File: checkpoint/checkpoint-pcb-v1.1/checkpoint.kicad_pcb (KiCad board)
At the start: 4 copper layers, 85.2 x 39.6 mm, 111 parts, among them J1 T0, J10 CAN_OUT, J11 BOOT, J12 Y_ENDSTOP, J13 SERVO, J14 RGB, J15 SWD, J16 USB_C_Receptacle_USB2.0_16P, J17 PWR_CAN_IN, J18 PWR_OUT, J19 I2C, J2 T1, J3 T2, J4 T3, J5 2_WIRE, J6 24_3_WIRE_A, J7 PT100, J8 23_WIRE, J9 PT100_1K, Q1 BSS138, SW1 SW_RESET, U1 MAX31865xTP, U2 SN65HVD1050D, U3 STM32G0B1CBTx, U4 USBLC6-2P6, U5 AMS1117-3.3, U6 TPS5430DDA, Y1 Crystal

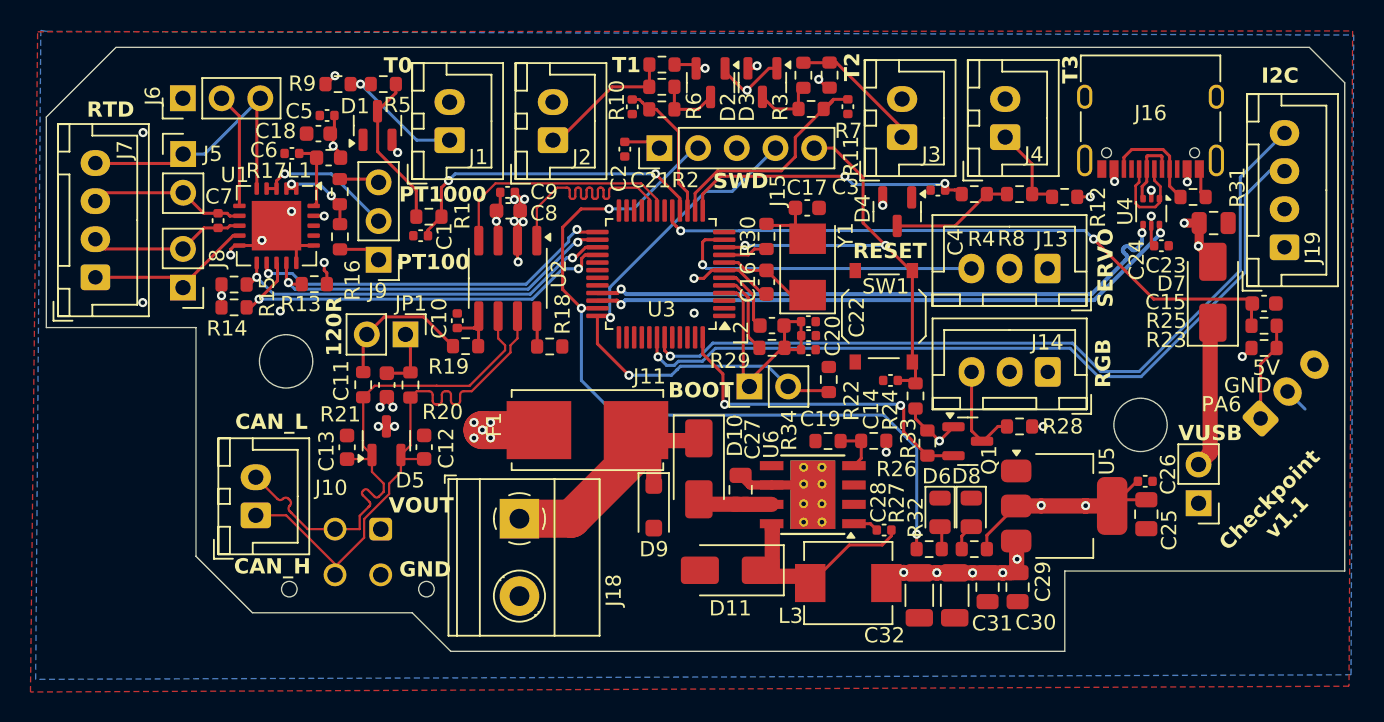
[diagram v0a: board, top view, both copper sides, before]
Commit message: chore: clear space around mount holes
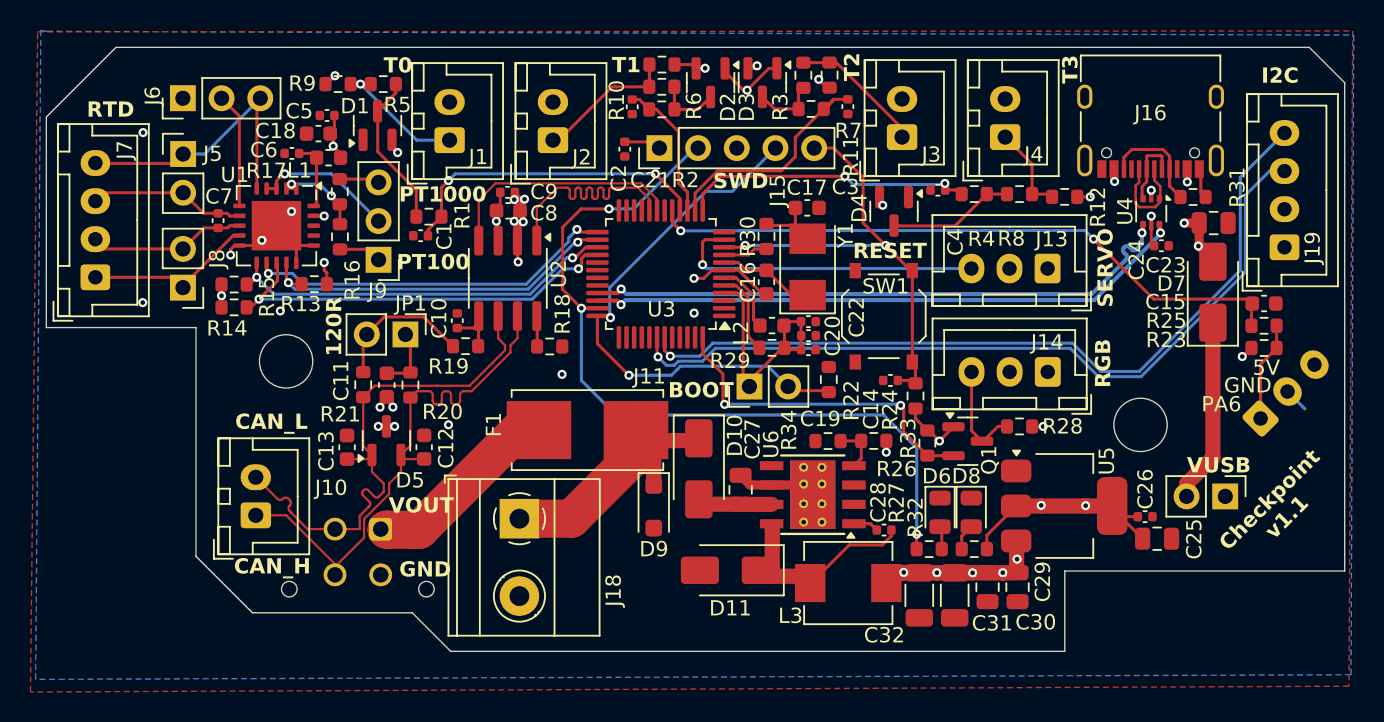
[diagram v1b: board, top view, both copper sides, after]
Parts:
- moved C26 2.32 mm to (94.3, 64.9)
- moved JP2 1.81 mm to (99.5, 63.5), turned to -90 degrees
- moved C25 1.76 mm to (95.1, 66.3), turned to 0 degrees
- moved D4 0.21 mm to (77.8, 44.8)
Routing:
- net VIN: track 3.72 -> 12.7 mm, vias 5 -> 0
- net Net-(D7-K): track 9.62 -> 12.2 mm
- net +3.3V: track 110.3 -> 111.6 mm
- net GND: track 33.8 -> 34.1 mm, vias 19 -> 21
- removed copper zone on In1.Cu, net VIN

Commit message: fix: rotate backwards filter diode
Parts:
- moved D10 0.23 mm to (65.0, 61.9), turned to 90 degrees
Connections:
- C27 pad 1: Net-(D10-A) -> Net-(D10-K)
- D10 pad 1: VOUT -> Net-(D10-K)
- D10 pad 2: Net-(D10-A) -> VOUT
- U6 pad 7: Net-(D10-A) -> Net-(D10-K)
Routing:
- net Net-(D10-K): track 0.00 -> 4.19 mm
- net Net-(D10-A): track 4.19 -> 0.00 mm
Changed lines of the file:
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@@
 	(net 21 "Net-(D4-COM)")
 	(net 22 "Net-(D8-A)")
-	(net 23 "Net-(D10-A)")
+	(net 23 "Net-(D10-K)")
 	(net 24 "Net-(J1-Pin_1)")
 	(net 25 "Net-(J2-Pin_1)")
@@
 		(tags "capacitor")
 		(property "Reference" "C27"
-			(at 3.33 0.79 -90)
+			(at 3.34 0.81 -90)
 			(layer "F.SilkS")
 			(effects
@@
 			(layers "F.Cu" "F.Paste" "F.Mask")
 			(roundrect_rratio 0.25)
-			(net 23 "Net-(D10-A)")
+			(net 23 "Net-(D10-K)")
 			(pintype "passive")
 		)
@@
 	(footprint "Diode_SMD:D_SMA"
 		(layer "F.Cu")
-		(at 64.980408 61.721118 -90)
+		(at 64.980408 61.948618 90)
 		(descr "Diode SMA (DO-214AC)")
 		(tags "Diode SMA (DO-214AC)")
 		(property "Reference" "D10"
-			(at -2.18 -2.37 -90)
+			(at 2.1375 2.35 -90)
 			(layer "F.SilkS")
 			(effects
@@
 		)
 		(property "Value" "SS34"
-			(at 0 2.6 90)
+			(at 0 2.6 -90)
 			(layer "F.Fab")
 			(effects
@@
 		)
 		(property "Footprint" "Diode_SMD:D_SMA"
-			(at 0 0 -90)
+			(at 0 0 90)
 			(unlocked yes)
 			(layer "F.Fab")
@@
 		)
 		(property "Datasheet" ""
-			(at 0 0 -90)
+			(at 0 0 90)
 			(unlocked yes)
 			(layer "F.Fab")
@@
 		)
 		(property "Description" "40V 3A Schottky Diode, SMA"
-			(at 0 0 -90)
+			(at 0 0 90)
 			(unlocked yes)
 			(layer "F.Fab")
@@
 		)
 		(property "Availability" ""
-			(at 0 0 -90)
+			(at 0 0 90)
 			(unlocked yes)
 			(layer "F.Fab")
@@
 		)
 		(property "Check_prices" ""
-			(at 0 0 -90)
+			(at 0 0 90)
 			(unlocked yes)
 			(layer "F.Fab")
@@
 		)
 		(property "Description_1" ""
-			(at 0 0 -90)
+			(at 0 0 90)
 			(unlocked yes)
 			(layer "F.Fab")
@@
 		)
 		(property "MF" ""
-			(at 0 0 -90)
+			(at 0 0 90)
 			(unlocked yes)
 			(layer "F.Fab")
@@
 		)
 		(property "MP" ""
-			(at 0 0 -90)
+			(at 0 0 90)
 			(unlocked yes)
 			(layer "F.Fab")
@@
 		)
 		(property "Package" ""
-			(at 0 0 -90)
+			(at 0 0 90)
 			(unlocked yes)
 			(layer "F.Fab")
@@
 		)
 		(property "Price" ""
-			(at 0 0 -90)
+			(at 0 0 90)
 			(unlocked yes)
 			(layer "F.Fab")
@@
 		)
 		(property "Purchase-URL" ""
-			(at 0 0 -90)
+			(at 0 0 90)
 			(unlocked yes)
 			(layer "F.Fab")
@@
 		)
 		(property "SnapEDA_Link" ""
-			(at 0 0 -90)
+			(at 0 0 90)
 			(unlocked yes)
 			(layer "F.Fab")
@@
 		)
 		(property "MANUFACTURER" ""
-			(at 0 0 -90)
+			(at 0 0 90)
 			(unlocked yes)
 			(layer "F.Fab")
@@
 		)
 		(property "MAXIMUM_PACKAGE_HEIGHT" ""
-			(at 0 0 -90)
+			(at 0 0 90)
 			(unlocked yes)
 			(layer "F.Fab")
@@
 		)
 		(property "PARTREV" ""
-			(at 0 0 -90)
+			(at 0 0 90)
 			(unlocked yes)
 			(layer "F.Fab")
@@
 		)
 		(property "SNAPEDA_PN" ""
-			(at 0 0 -90)
+			(at 0 0 90)
 			(unlocked yes)
 			(layer "F.Fab")
@@
 		)
 		(property "STANDARD" ""
-			(at 0 0 -90)
+			(at 0 0 90)
 			(unlocked yes)
 			(layer "F.Fab")
@@
 		(attr smd)
 		(fp_line
-			(start -3.51 1.65)
-			(end 2 1.65)
+			(start -3.51 -1.65)
+			(end 2 -1.65)
 			(stroke
 				(width 0.12)
@@
 		)
 		(fp_line
-			(start -3.51 -1.65)
-			(end 2 -1.65)
+			(start -3.51 1.65)
+			(end 2 1.65)
 			(stroke
 				(width 0.12)
@@
 		)
 		(fp_line
-			(start -3.5 1.75)
-			(end -3.5 -1.75)
+			(start 3.5 -1.75)
+			(end 3.5 1.75)
 			(stroke
 				(width 0.05)
@@
 		)
 		(fp_line
-			(start 3.5 1.75)
-			(end -3.5 1.75)
+			(start -3.5 -1.75)
+			(end 3.5 -1.75)
 			(stroke
 				(width 0.05)
@@
 		)
 		(fp_line
-			(start -3.5 -1.75)
-			(end 3.5 -1.75)
+			(start 3.5 1.75)
+			(end -3.5 1.75)
 			(stroke
 				(width 0.05)
@@
 		)
 		(fp_line
-			(start 3.5 -1.75)
-			(end 3.5 1.75)
+			(start -3.5 1.75)
+			(end -3.5 -1.75)
 			(stroke
 				(width 0.05)
@@
 		)
 		(fp_line
-			(start -2.3 1.5)
+			(start 2.3 -1.5)
 			(end -2.3 -1.5)
 			(stroke
@@
 		)
 		(fp_line
-			(start 2.3 1.5)
-			(end -2.3 1.5)
+			(start 2.3 -1.5)
+			(end 2.3 1.5)
 			(stroke
 				(width 0.1)
@@
 		)
 		(fp_line
-			(start 0.50118 0.75032)
-			(end 0.50118 -0.79908)
+			(start -0.64944 -0.79908)
+			(end -0.64944 0.80112)
 			(stroke
 				(width 0.1)
@@
 		)
 		(fp_line
-			(start -0.64944 0.00102)
-			(end 0.50118 0.75032)
+			(start 0.50118 0.00102)
+			(end 1.4994 0.00102)
 			(stroke
 				(width 0.1)
@@
 		(fp_line
 			(start -0.64944 0.00102)
-			(end -1.55114 0.00102)
+			(end 0.50118 -0.79908)
 			(stroke
 				(width 0.1)
@@
 		(fp_line
 			(start -0.64944 0.00102)
-			(end 0.50118 -0.79908)
+			(end -1.55114 0.00102)
 			(stroke
 				(width 0.1)
@@
 		)
 		(fp_line
-			(start 0.50118 0.00102)
-			(end 1.4994 0.00102)
+			(start -0.64944 0.00102)
+			(end 0.50118 0.75032)
 			(stroke
 				(width 0.1)
@@
 		)
 		(fp_line
-			(start -0.64944 -0.79908)
-			(end -0.64944 0.80112)
+			(start 0.50118 0.75032)
+			(end 0.50118 -0.79908)
 			(stroke
 				(width 0.1)
@@
 		)
 		(fp_line
-			(start 2.3 -1.5)
-			(end 2.3 1.5)
+			(start 2.3 1.5)
+			(end -2.3 1.5)
 			(stroke
 				(width 0.1)
@@
 		)
 		(fp_line
-			(start 2.3 -1.5)
+			(start -2.3 1.5)
 			(end -2.3 -1.5)
 			(stroke
@@
 		)
 		(fp_text user "${REFERENCE}"
-			(at 0 -2.5 90)
+			(at 0 -2.5 -90)
 			(layer "F.Fab")
 			(effects
@@
 		)
 		(pad "1" smd roundrect
-			(at -2 0 270)
+			(at -2 0 90)
 			(size 2.5 1.8)
 			(layers "F.Cu" "F.Paste" "F.Mask")
 			(roundrect_rratio 0.1388888889)
-			(net 92 "VOUT")
+			(net 23 "Net-(D10-K)")
 			(pinfunction "K")
 			(pintype "passive")
 		)
 		(pad "2" smd roundrect
-			(at 2 0 270)
+			(at 2 0 90)
 			(size 2.5 1.8)
 			(layers "F.Cu" "F.Paste" "F.Mask")
 			(roundrect_rratio 0.1388888889)
-			(net 23 "Net-(D10-A)")
+			(net 92 "VOUT")
 			(pinfunction "A")
 			(pintype "passive")
@@
 		)
 		(property "Value" "22uF"
-			(at -0.05 1.35 360)
+			(at -0.05 1.35 0)
 			(layer "F.Fab")
 			(effects
@@
 		)
 		(fp_text user "${REFERENCE}"
-			(at 0 0 360)
+			(at 0 0 0)
 			(layer "F.Fab")
 			(effects
@@
 			(size 1.55 0.6)
 			(layers "F.Cu" "F.Paste" "F.Mask")
-			(net 23 "Net-(D10-A)")
+			(net 23 "Net-(D10-K)")
 			(pinfunction "VIN")
 			(pintype "power_in")

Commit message: chore: reset refdes numbers
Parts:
- renumbered C18 to C16, C16 to C17, C19 to C18, C21 to C19, C17 to C20, C20 to C21, J19 to J11, J11 to J12, J12 to J13, J13 to J14, J14 to J15, J15 to J16, J16 to J17, J17 to J19, R23 to R22, R22 to R23, R27 to R26, R29 to R27, R26 to R28, R28 to R29

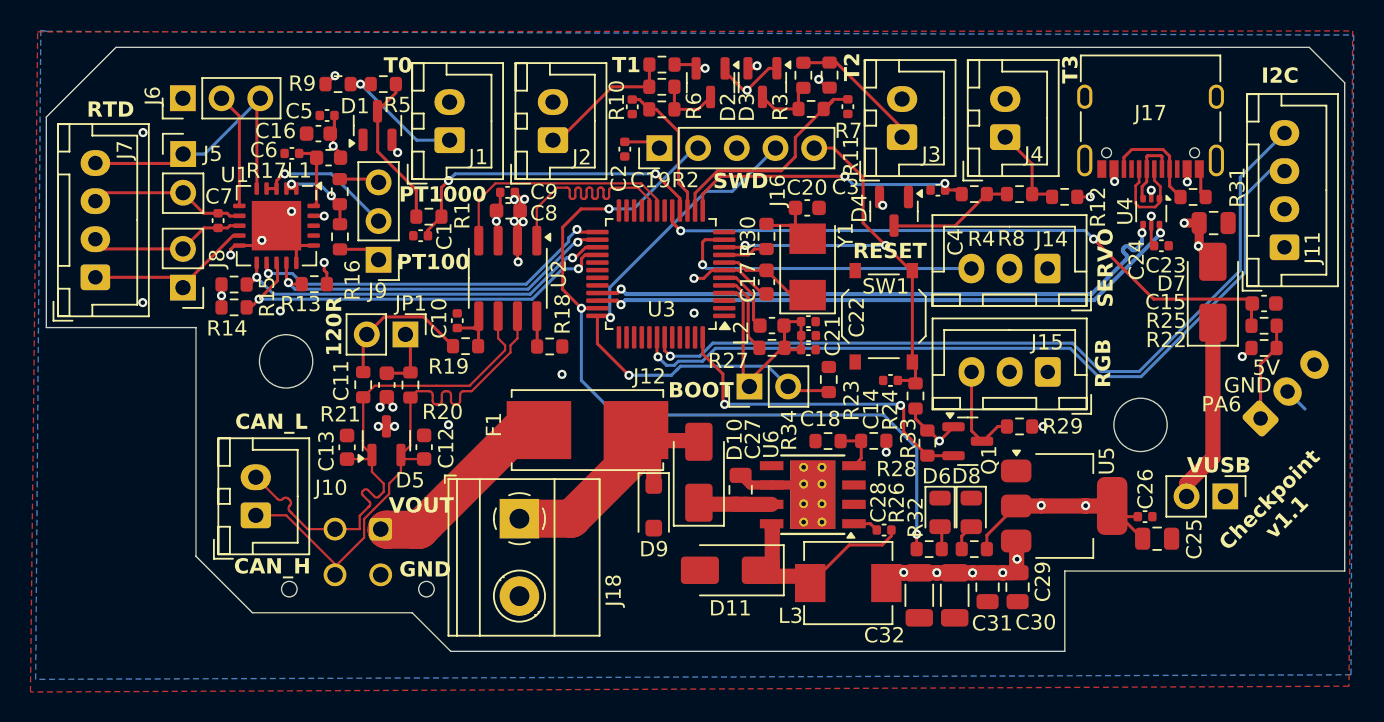
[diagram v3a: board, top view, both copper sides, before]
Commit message: fix: add i2c pullup resistors
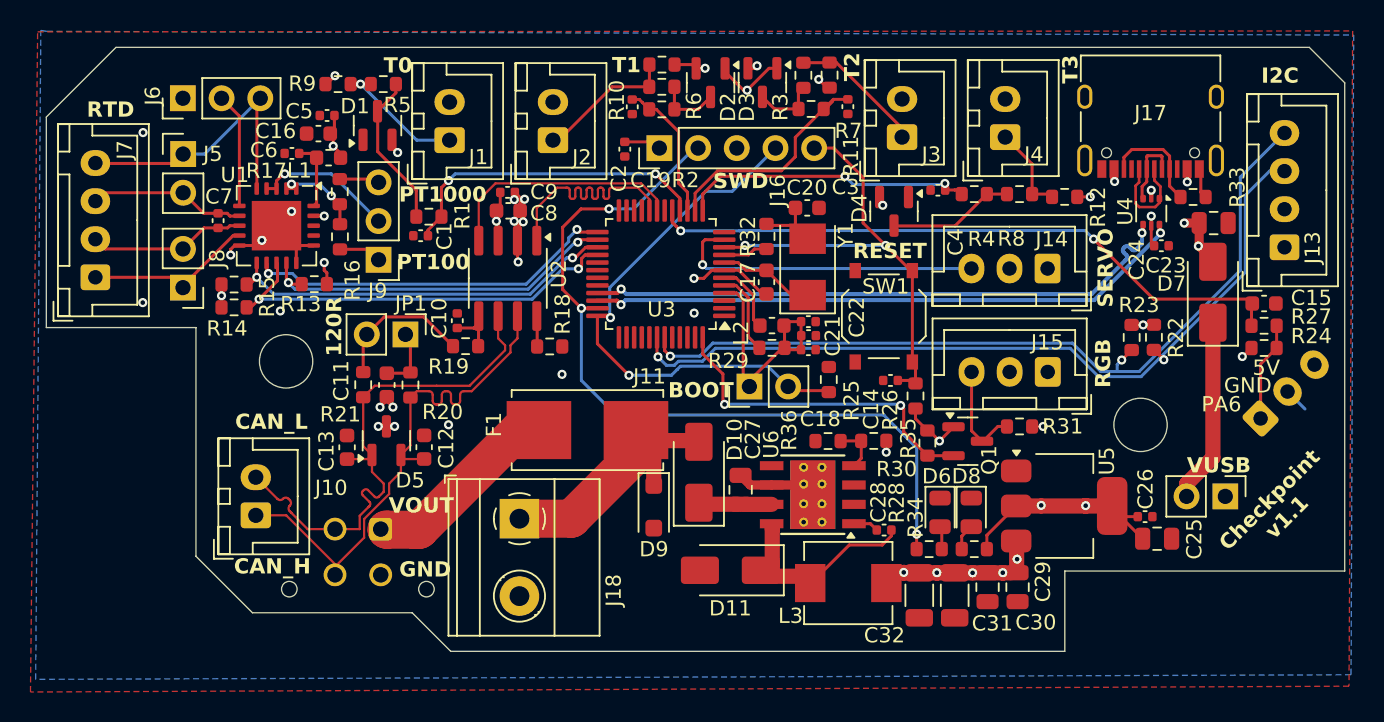
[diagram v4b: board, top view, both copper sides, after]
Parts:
- added R22: 4.7K, Resistor_SMD:R_0603_1608Metric, F.Cu at (94.9, 53.1)
- added R23: 4.7K, Resistor_SMD:R_0603_1608Metric, F.Cu at (93.4, 53.1)
- renumbered J12 to J11, J13 to J12, J11 to J13, R22 to R24, R23 to R25, R24 to R26, R25 to R27, R26 to R28, R27 to R29, R28 to R30, R29 to R31, R30 to R32, R31 to R33, R32 to R34, R33 to R35, R34 to R36
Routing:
- net +3.3V: track 111.6 -> 120.5 mm, vias 15 -> 16
- net I2C_SDA: track 52.9 -> 54.7 mm, vias 1 -> 2
- net I2C_SCL: track 52.4 -> 53.7 mm, vias 1 -> 2

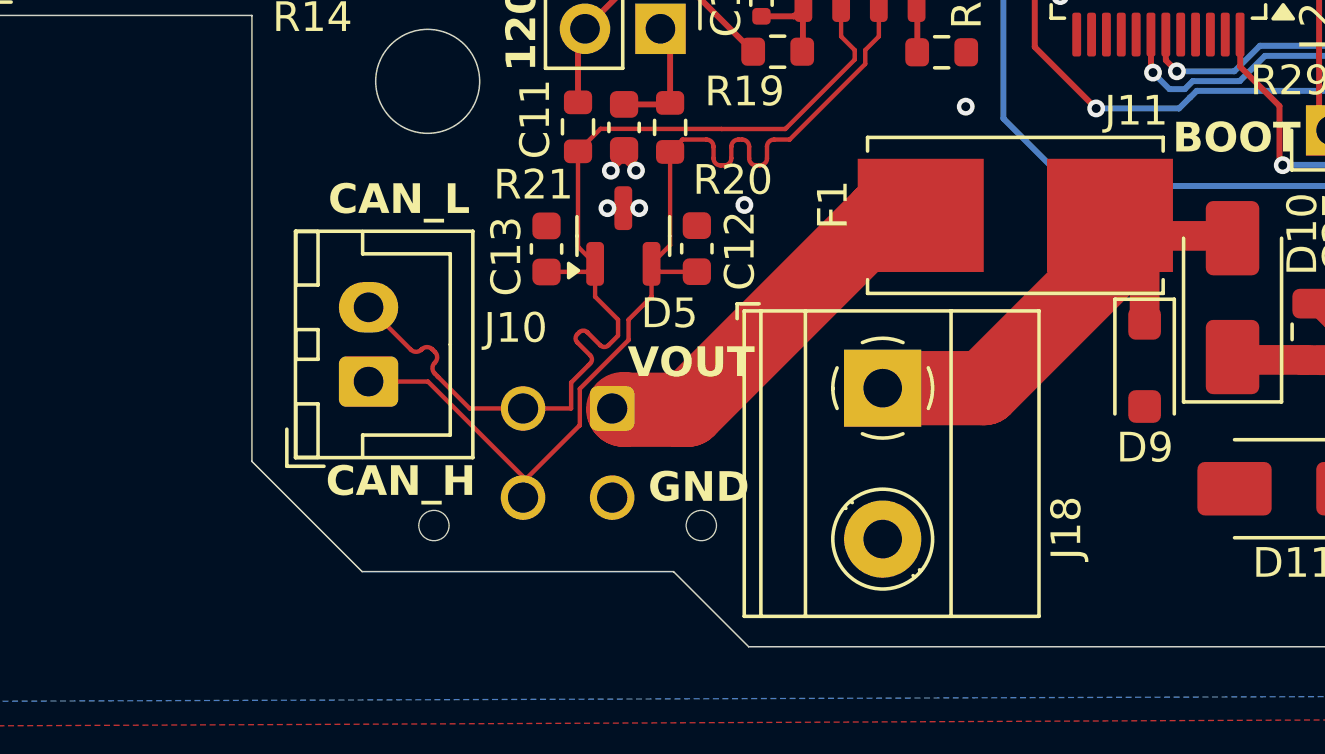
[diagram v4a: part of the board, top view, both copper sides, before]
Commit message: fix: swap can lines to match BTT convention
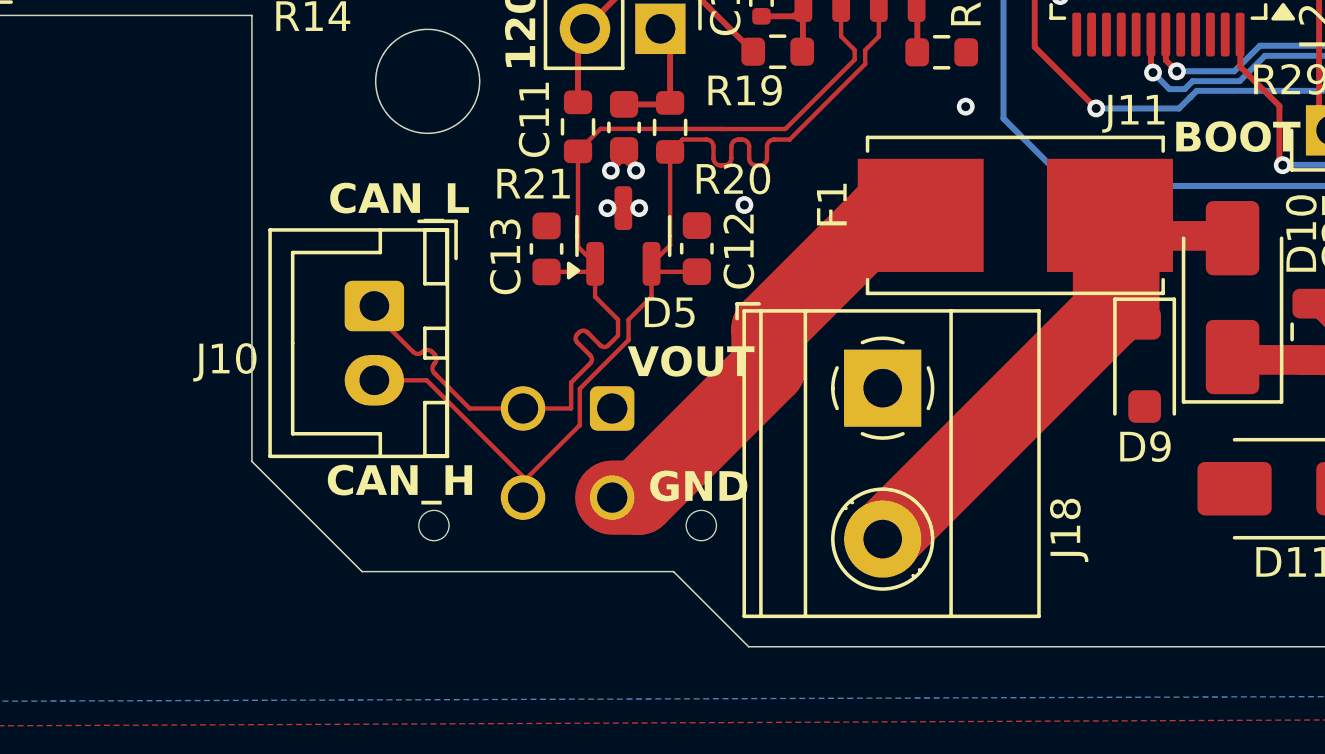
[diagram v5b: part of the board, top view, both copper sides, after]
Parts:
- moved J10 2.55 mm to (36.1, 62.2), turned to -90 degrees
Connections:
- J10 pad 1: CAN_P -> CAN_N
- J10 pad 2: CAN_N -> CAN_P
- J18 pad 1: VOUT -> GND
- J18 pad 2: GND -> VOUT
- J19 pad 1: VIN -> GND
- J19 pad 3: GND -> VIN
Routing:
- net VOUT: track 16.9 -> 20.0 mm
- net VIN: track 12.7 -> 15.1 mm

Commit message: chore: switch to vertical usb-c port
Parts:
- J17: footprint Connector_USB:USB_C_Receptacle_XKB_U262-16XN-4BVC11 -> Library:USB_C_14P_VERT_XUNPU
- moved R33 7.81 mm to (94.7, 36.6)
- moved J17 1.82 mm to (94.7, 40.2), turned to 0 degrees
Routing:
- net VBUS: track 7.34 -> 20.2 mm, vias 5 -> 3
- net I2C_SDA: track 54.7 -> 52.3 mm
- net I2C_SCL: track 53.7 -> 51.3 mm
- net GND: track 34.1 -> 32.1 mm
- net D_P: track 6.45 -> 5.16 mm
- net Net-(J17-CC1): track 7.14 -> 7.80 mm

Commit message: chore: add hidden jlcpcb order number token
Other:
- board text added: "JLCJLCJLCJLC"
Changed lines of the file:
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@@
 		(tags "connector JST XH vertical")
 		(property "Reference" "J7"
-			(at 8.361118 1.929592 -90)
+			(at -1.67 -0.9 -90)
 			(layer "F.SilkS")
 			(effects
@@
 			)
 			(justify left bottom)
+		)
+	)
+	(gr_text "JLCJLCJLCJLC"
+		(at 28.010408 50.711118 90)
+		(layer "F.SilkS")
+		(effects
+			(font
+				(size 1 1)
+				(thickness 0.15)
+			)
+			(justify left bottom)
